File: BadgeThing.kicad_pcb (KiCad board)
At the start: 2 copper layers, 65 parts, among them J1 USB_C_Receptacle_USB2.0, J2 Connector_Generic_Conn_01x02, J3 Ext 5V, J4 SWD Header, J6 Conn_01x07, J7 Conn_01x07, J8 Conn_01x08, SW1 BOOTSEL, SW2 ESP RESET, SW3 Left, SW4 Down, SW5 Select, SW6 Up, SW7 Right, U2 W25Q32JVSS, U3 RP2040, U4 NCP1117-3.3_SOT223, U5 ESP-12F, Y1 12.000MHz

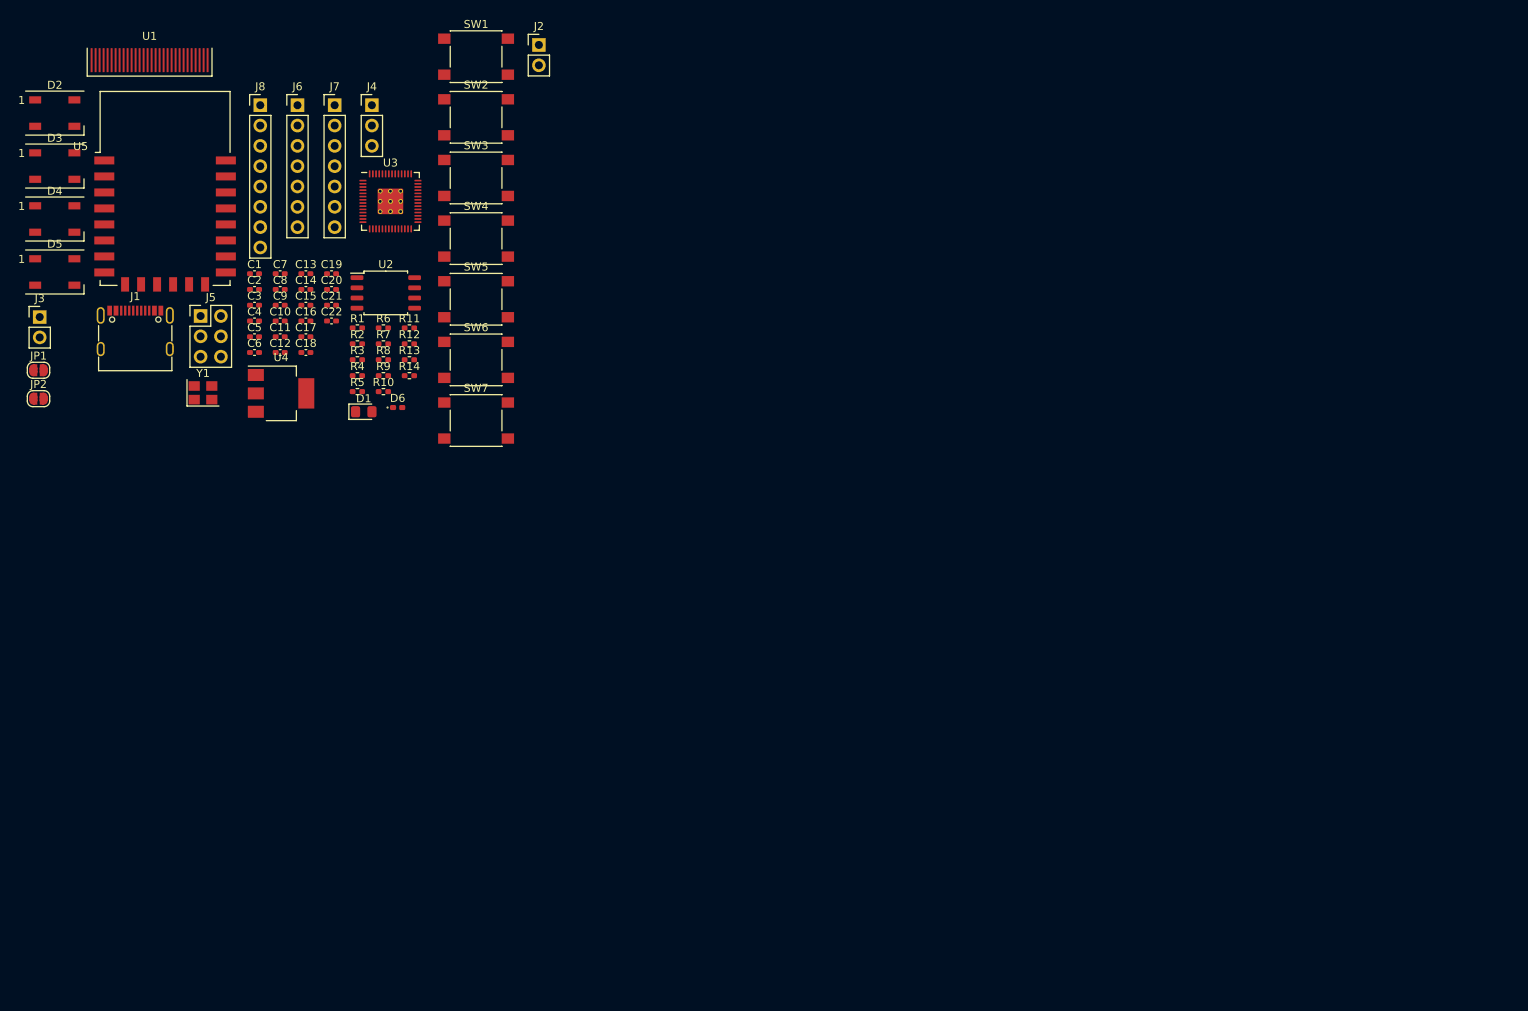
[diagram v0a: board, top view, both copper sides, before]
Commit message: RP2040/OLED circuits, basic component placement
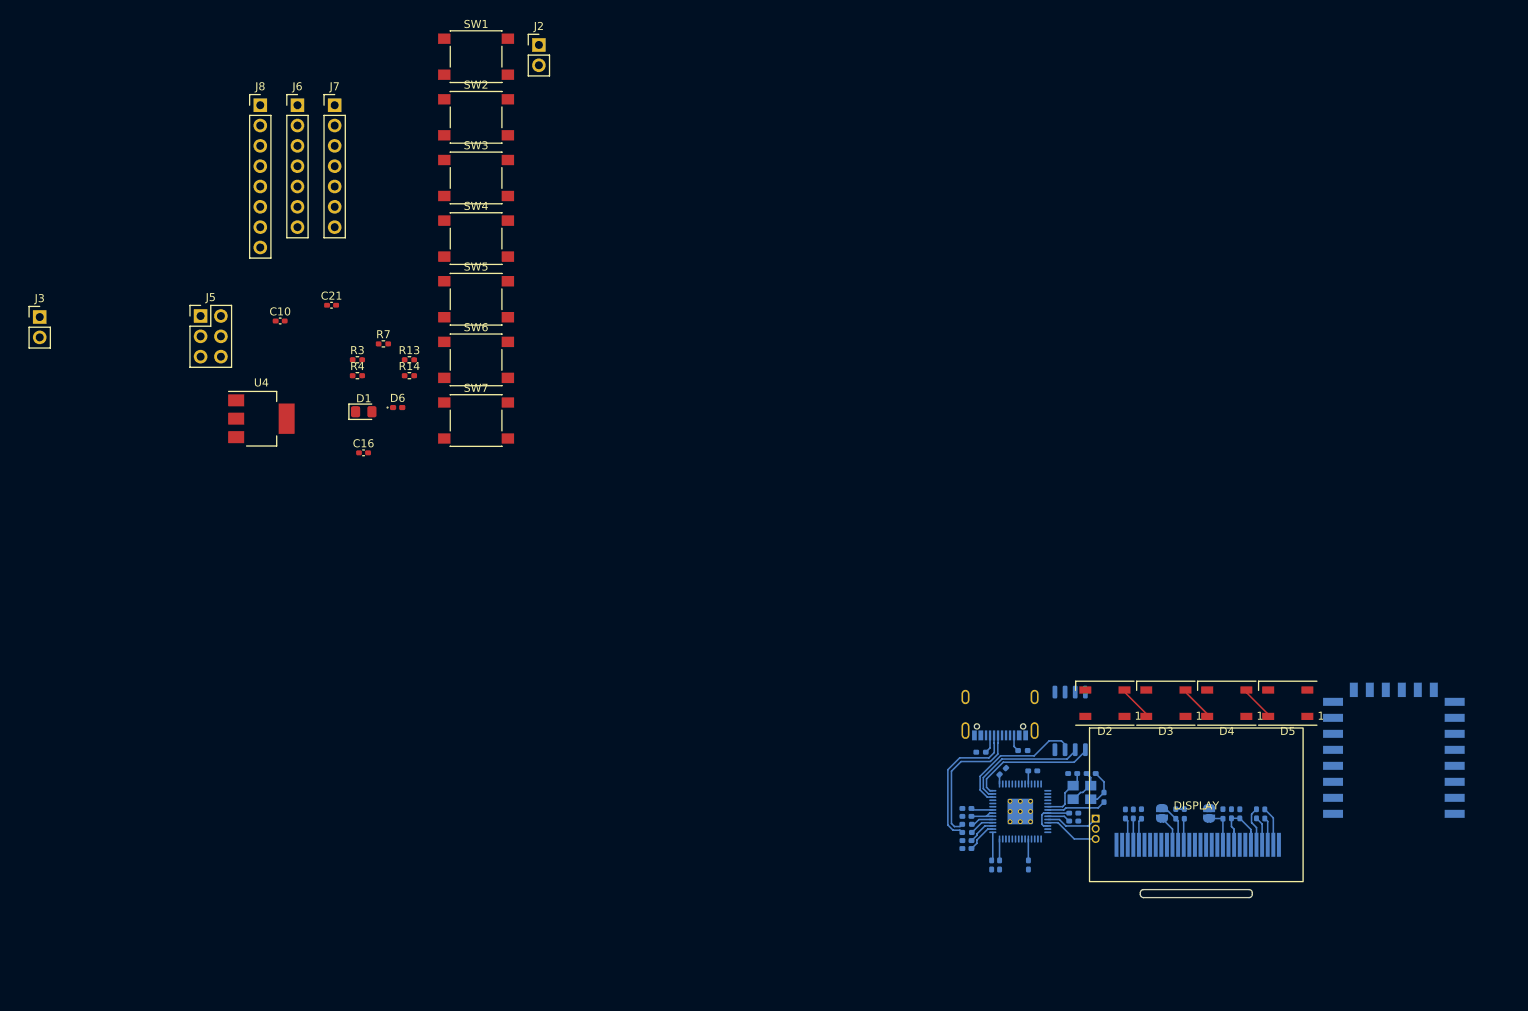
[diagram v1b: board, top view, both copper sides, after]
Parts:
- C1, C11, C12, C13, C14, C15, C17, C18, C19, C2, C20, C22, C3, C4, C5, C6, C7, C8, C9, J1, JP1, JP2, R1, R10, R11, R12, R2, R5, R6, R8, R9, U2, U3, U5, Y1: moved to B.Cu
- J4: footprint Connector_PinHeader_2.54mm:PinHeader_1x03_P2.54mm_Vertical -> Connector_PinHeader_1.27mm:PinHeader_1x03_P1.27mm_Vertical; moved to B.Cu
- moved U5 170.8 mm to (186.4, 108.0)
- moved D5 163.3 mm to (173.2, 97.7), turned to 180 degrees
- moved U1 160.6 mm to (161.7, 110.4)
- moved D4 158.5 mm to (165.6, 97.7), turned to 180 degrees
- moved JP1 156.5 mm to (163.3, 111.4), turned to -90 degrees
- moved D3 154.3 mm to (157.9, 97.7), turned to 180 degrees
- moved D2 150.6 mm to (150.3, 97.7), turned to 180 degrees
- moved JP2 149.7 mm to (157.5, 111.4), turned to -90 degrees
- moved C1 143.2 mm to (170.3, 111.5), turned to 90 degrees
- moved C2 141.4 mm to (169.3, 111.5), turned to -90 degrees
- moved C4 137.7 mm to (167.2, 111.5), turned to -90 degrees
- moved C3 137.7 mm to (166.1, 111.5), turned to -90 degrees
- moved J4 127.0 mm to (149.2, 112.1), turned to 180 degrees
- moved C5 125.0 mm to (153.9, 111.5), turned to -90 degrees
- moved R1 124.1 mm to (165.1, 111.5), turned to 90 degrees
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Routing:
- net +3V3: track 0.00 -> 37.6 mm
- net USB D-: track 0.00 -> 17.9 mm
- net USB D+: track 0.00 -> 17.2 mm
- net QSPI_SD2: track 0.00 -> 17.0 mm
- net QSPI_SS: track 0.00 -> 16.0 mm
- net QSPI_SD1: track 0.00 -> 15.9 mm
- net +1V1: track 0.00 -> 9.19 mm
- net XOUT: track 0.00 -> 7.43 mm
- net SWDIO: track 0.00 -> 6.82 mm
- net XIN: track 0.00 -> 6.82 mm
- net SWCLK: track 0.00 -> 6.70 mm
- net MOSI: track 0.00 -> 5.66 mm
- net Net-(JP1-B): track 0.00 -> 5.00 mm
- net Net-(U1-C1N): track 0.00 -> 4.95 mm
- net Net-(U1-C2P): track 0.00 -> 4.87 mm
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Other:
- board outline added: 14 x 1 mm

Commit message: more routing + layout
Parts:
- C10, C16, C21, D1, R13, R14, R3, R4, R7, SW1, SW2, U4: moved to B.Cu
- D6: value Greeen -> Green; moved to B.Cu
- moved J5 170.3 mm to (189.0, 126.7), turned to -90 degrees
- moved J2 125.8 mm to (141.5, 124.8)
- moved SW2 124.6 mm to (170.9, 99.9), turned to -90 degrees
- moved R13 123.8 mm to (175.9, 106.5)
- moved SW7 123.6 mm to (176.4, 128.0), turned to 90 degrees
- moved SW1 123.6 mm to (163.2, 99.9), turned to -90 degrees
- moved R14 122.2 mm to (175.9, 104.5)
- moved SW3 122.0 mm to (147.0, 128.0), turned to 90 degrees
- moved SW6 121.8 mm to (169.1, 128.0), turned to 90 degrees
- moved SW4 121.0 mm to (154.3, 128.0), turned to 90 degrees
- moved SW5 121.0 mm to (161.7, 128.0), turned to 90 degrees
- moved R3 119.8 mm to (165.4, 105.5), turned to 180 degrees
- moved J3 119.7 mm to (127.5, 95.8), turned to 90 degrees
- moved U4 116.9 mm to (155.5, 99.9), turned to -90 degrees
- moved C10 112.7 mm to (149.9, 96.3), turned to -90 degrees
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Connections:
- D2 pad 1: +3V3 -> +5V
- D3 pad 1: +3V3 -> +5V
- D4 pad 1: +3V3 -> +5V
- D5 pad 1: +3V3 -> +5V
- U3 pad 11: BTN2 -> unconnected-(U3-GPIO8-Pad11)
- U3 pad 12: BTN3 -> unconnected-(U3-GPIO9-Pad12)
- U3 pad 13: BTN4 -> unconnected-(U3-GPIO10-Pad13)
- U3 pad 14: BTN5 -> unconnected-(U3-GPIO11-Pad14)
- U3 pad 17: WS2812B -> SCLK
- U3 pad 18: GP15 -> MOSI
- U3 pad 2: DC -> unconnected-(U3-GPIO0-Pad2)
- U3 pad 27: GP16 -> MISO
- U3 pad 28: GP17 -> DC
- U3 pad 29: GP18 -> RST
- U3 pad 3: RST -> unconnected-(U3-GPIO1-Pad3)
- U3 pad 30: GP19 -> CS1
- U3 pad 31: GP20 -> BTN5
- U3 pad 32: GP21 -> BTN4
- U3 pad 34: GP22 -> BTN3
- U3 pad 35: GP23 -> BTN2
- U3 pad 36: GP24 -> BTN1
- U3 pad 38: GP26 -> unconnected-(U3-GPIO26_ADC0-Pad38)
- U3 pad 39: GP27 -> unconnected-(U3-GPIO27_ADC1-Pad39)
- U3 pad 4: SCLK -> unconnected-(U3-GPIO2-Pad4)
- U3 pad 40: GP28 -> unconnected-(U3-GPIO28_ADC2-Pad40)
- U3 pad 41: GP29 -> unconnected-(U3-GPIO29_ADC3-Pad41)
- U3 pad 5: MOSI -> unconnected-(U3-GPIO3-Pad5)
- U3 pad 6: MISO -> unconnected-(U3-GPIO4-Pad6)
- U3 pad 7: CS1 -> unconnected-(U3-GPIO5-Pad7)
- U3 pad 9: BTN1 -> unconnected-(U3-GPIO7-Pad9)
- U5 pad 16: ESP15 -> unconnected-(U5-GPIO15-Pad16)
- U5 pad 17: ESP2 -> unconnected-(U5-GPIO2-Pad17)
- U5 pad 19: ESP4 -> unconnected-(U5-GPIO4-Pad19)
- U5 pad 20: ESP5 -> unconnected-(U5-GPIO5-Pad20)
- U5 pad 4: ESP16 -> unconnected-(U5-GPIO16-Pad4)
- U5 pad 5: ESP14 -> unconnected-(U5-GPIO14-Pad5)
- U5 pad 6: ESP12 -> unconnected-(U5-GPIO12-Pad6)
- U5 pad 7: ESP13 -> unconnected-(U5-GPIO13-Pad7)
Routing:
- net +5V: track 0.00 -> 71.7 mm, vias 0 -> 4
- net BTN5: track 0.00 -> 50.2 mm, vias 0 -> 1
- net BTN4: track 0.00 -> 41.9 mm, vias 0 -> 1
- net BTN3: track 0.00 -> 36.7 mm, vias 0 -> 1
- net +3V3: track 37.6 -> 73.4 mm
- net BTN2: track 0.00 -> 29.8 mm, vias 0 -> 1
- net Net-(U5-~{RST}): track 0.00 -> 29.2 mm
- net QSPI_SD3: track 0.00 -> 28.9 mm
- net ESP_TX: track 0.00 -> 28.2 mm
- net QSPI_SCLK: track 0.00 -> 26.1 mm
- net CS1: track 0.00 -> 25.7 mm
- net ESP_RX: track 0.00 -> 25.2 mm
- net SCLK: track 3.29 -> 27.6 mm
- net RST: track 0.00 -> 24.2 mm
- net BTN1: track 0.00 -> 23.9 mm, vias 0 -> 1
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- added copper zone on B.Cu, net GND
- added copper zone on F.Cu, net GND
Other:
- board size 14 x 1 mm -> 78.7 x 40.2 mm
- board text added: "BEEPER"
- board text added: "BOOT"
- board text added: "ESP ICSP"
- board text added: "ESP RST"
- board text added: "SEL"

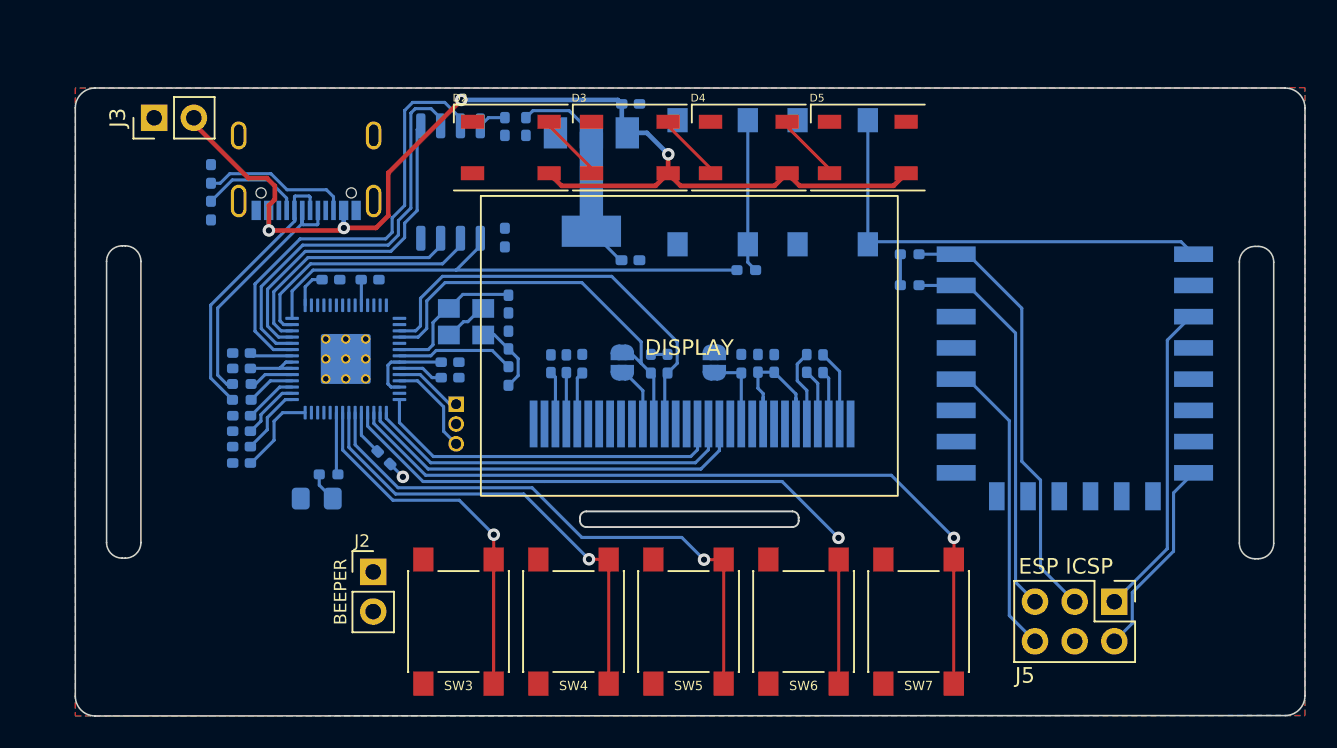
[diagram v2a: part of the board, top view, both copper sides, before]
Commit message: Completed initial routing
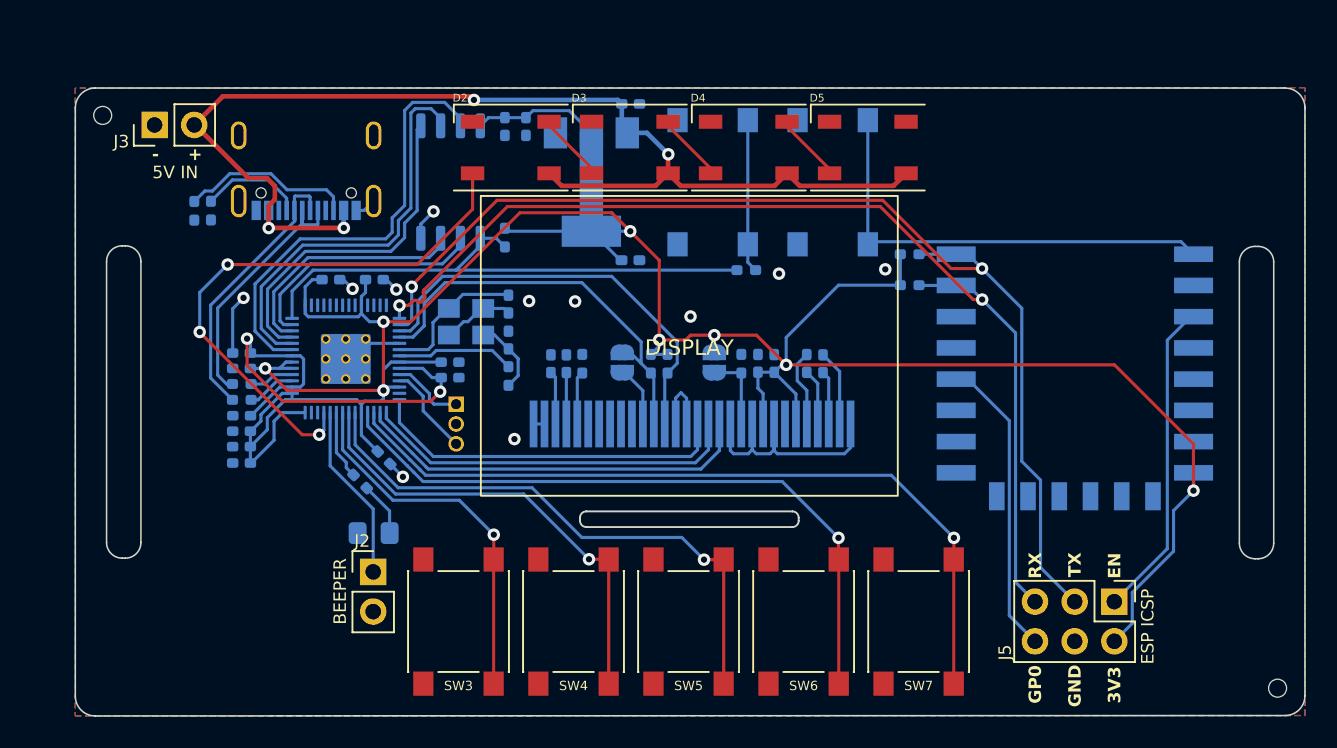
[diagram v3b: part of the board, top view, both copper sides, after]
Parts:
- added REF**: MountingHole_1.152mm, MountingHole:MountingHole_1.152mm, F.Cu at (124.2, 95.6)
- added REF**: MountingHole_1.152mm, MountingHole:MountingHole_1.152mm, F.Cu at (199.4, 132.3)
- moved D1 4.26 mm to (141.5, 122.4)
- moved R9 2.59 mm to (130.0, 101.7), turned to 90 degrees
- moved R7 2.07 mm to (140.7, 119.0), turned to -45 degrees
- moved J3 0.46 mm to (127.5, 96.2)
- moved C18 0.28 mm to (141.6, 106.1)
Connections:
- U3 pad 38: unconnected-(U3-GPIO26_ADC0-Pad38) -> BEEP
- U3 pad 39: unconnected-(U3-GPIO27_ADC1-Pad39) -> WS2812B
- U3 pad 8: BEEP -> unconnected-(U3-GPIO6-Pad8)
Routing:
- net +3V3: track 73.4 -> 189.9 mm, vias 0 -> 8
- net ESP_TX: track 28.2 -> 71.9 mm, vias 0 -> 2
- net ESP_RX: track 25.2 -> 68.9 mm, vias 0 -> 2
- net WS2812B: track 0.00 -> 36.4 mm, vias 0 -> 3
- net GND: track 4.06 -> 39.1 mm, vias 1 -> 11
- net +1V1: track 9.08 -> 29.6 mm, vias 0 -> 2
- net BEEP: track 0.00 -> 11.3 mm
- net +5V: track 71.7 -> 76.2 mm
- net QSPI_SS: track 33.5 -> 35.3 mm
- net Net-(D1-A): track 1.91 -> 3.49 mm
- net Net-(J1-CC2): track 9.58 -> 11.1 mm
- net BTN4: track 41.9 -> 43.3 mm
- net XIN: track 10.0 -> 9.30 mm
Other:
- board text added: "+"
- board text added: "-"
- board text added: "3V3"
- board text added: "5V IN"
- board text added: "BRIDGE JUMPERS TO CHANGE DISPLAY TO I2C MODE!"
- board text added: "EN"
- board text added: "GND"
- board text added: "GP0"
- board text added: "RX"
- board text added: "TX"

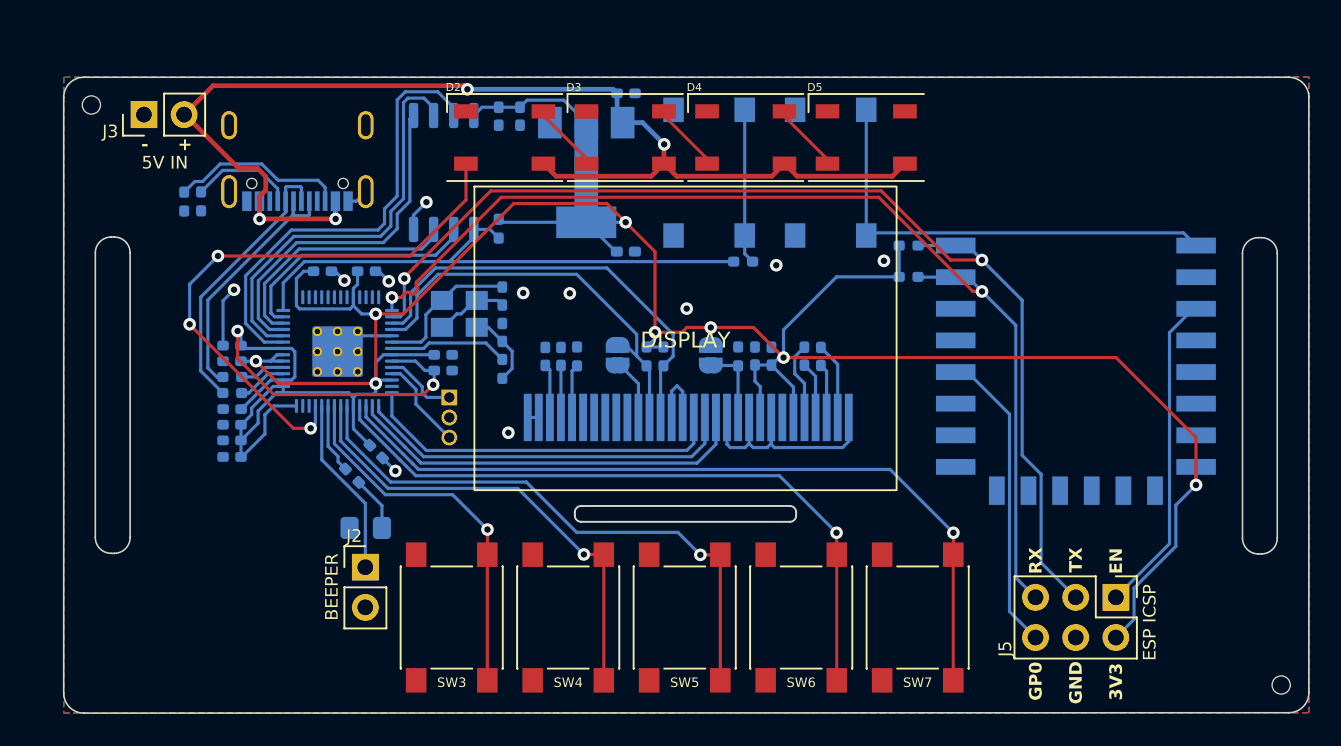
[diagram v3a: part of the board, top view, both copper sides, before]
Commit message: small tweaks, visual changes, added missing traces
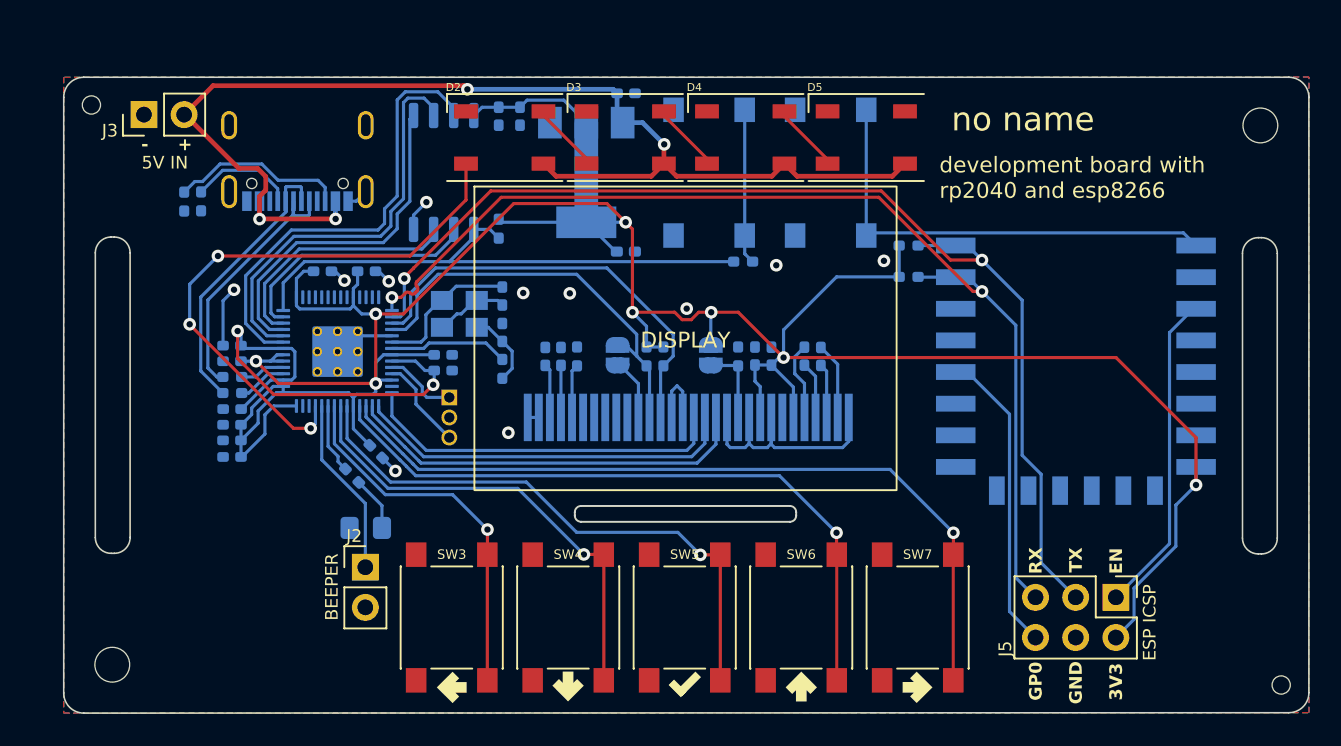
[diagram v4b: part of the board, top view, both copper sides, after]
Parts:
- added REF**: MountingHole_2.2mm_M2, MountingHole:MountingHole_2.2mm_M2, F.Cu at (198.1, 96.9)
- added REF**: MountingHole_2.2mm_M2, MountingHole:MountingHole_2.2mm_M2, F.Cu at (125.5, 131.0)
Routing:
- net +3V3: track 189.9 -> 192.5 mm
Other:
- board text added: "development board with rp2040 and esp8266"
- board text added: "no name"

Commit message: Layout tweaks + JLC part numbers
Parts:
- removed D6: Green, LED_SMD:LED_0402_1005Metric_Pad0.77x0.64mm_HandSolder
- removed J6, J7: Conn_01x07, Connector_PinHeader_2.54mm:PinHeader_1x07_P2.54mm_Vertical
- removed J8: Conn_01x08, Connector_PinHeader_2.54mm:PinHeader_1x08_P2.54mm_Vertical
- moved R3 0.23 mm to (165.6, 105.5)
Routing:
- net +3V3: track 192.5 -> 189.8 mm
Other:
- board text added: "128*64 OLED / SSD1306"
- board text added: "APPLY DOUBLE SIDED TAPE"
- board text added: "BRIDGE JUMPERS TO CHANGE DISPLAY TO I2C MODE! WIRES WILL HAVE TO BE BODGED. TRY AT YOUR OWN RISK."
- board text added: "DEBUG"
- board text added: "DISPLAY"
- board text added: "ESP8266"
- board text added: "EXTERNAL POWER"
- board text added: "RGB"
- board text added: "SWCLK"
- board text added: "SWDIO"
- board text removed: "5V IN"
- board text removed: "BRIDGE JUMPERS TO CHANGE DISPLAY TO I2C MODE!"
